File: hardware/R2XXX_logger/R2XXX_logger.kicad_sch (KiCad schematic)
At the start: 34 parts, among them U1 RP2350A, U4 W25Q16JVSS, U7 APS6404L-3SQRx-SN, X1 ABM8-272-T3

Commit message: Throws flatbuf packets
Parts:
- removed CC_19, CC_20: (no value), CC_Misc:CC_Current_Tester, symbol CC_Misc:CC_Current_Tester
- added R4, R5: 10k, Resistor_SMD:R_0603_1608Metric_Pad0.98x0.95mm_HandSolder, symbol Device:R
- added R6, R7: 27, Resistor_SMD:R_0603_1608Metric_Pad0.98x0.95mm_HandSolder, symbol Device:R
- renumbered C55 to C1, C56 to C10, C57 to C11, C58 to C12, C59 to C13, C60 to C14, C29 to C15, C30 to C16, C31 to C17, C34 to C18, C9 to C2, C26 to C3, C28 to C4, C1 to C5, C2 to C6, C42 to C7, C53 to C8, C45 to C9, GND_TP2 to GND_TP1, GND_TP1 to GND_TP2, R14 to R1, R5 to R2, R6 to R3, R3 to R8, U7 to U1, U4 to U2, U1 to U3
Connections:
- net RP_IO is gone; now on net +3.3V: C10.2, C11.2, C12.2, C13.2, C14.2, C9.2, U3.1 (IOVDD), U3.11 (IOVDD), U3.20 (IOVDD), U3.30 (IOVDD), U3.38 (IOVDD), U3.45 (IOVDD)
- net RP_PWR is gone; now on net +3.3V: C7.2, C8.2, R2.1, R3.1, U3.49 (VREG_VIN), U3.53 (USB_OTP_VDD), U3.54 (QSPI_IOVDD)
- net +3.3V: now also R4.2, R5.1
- net USB_DN: now also R7.2
- net USB_DP: now also R6.1; no longer U3.51 (USB_DM)
- net at U3.52 (USB_DP): now also R7.1
- new net: R6.2, U3.51 (USB_DM)
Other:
- moved on the sheet: C10, C11, C12, C13, C14, C9

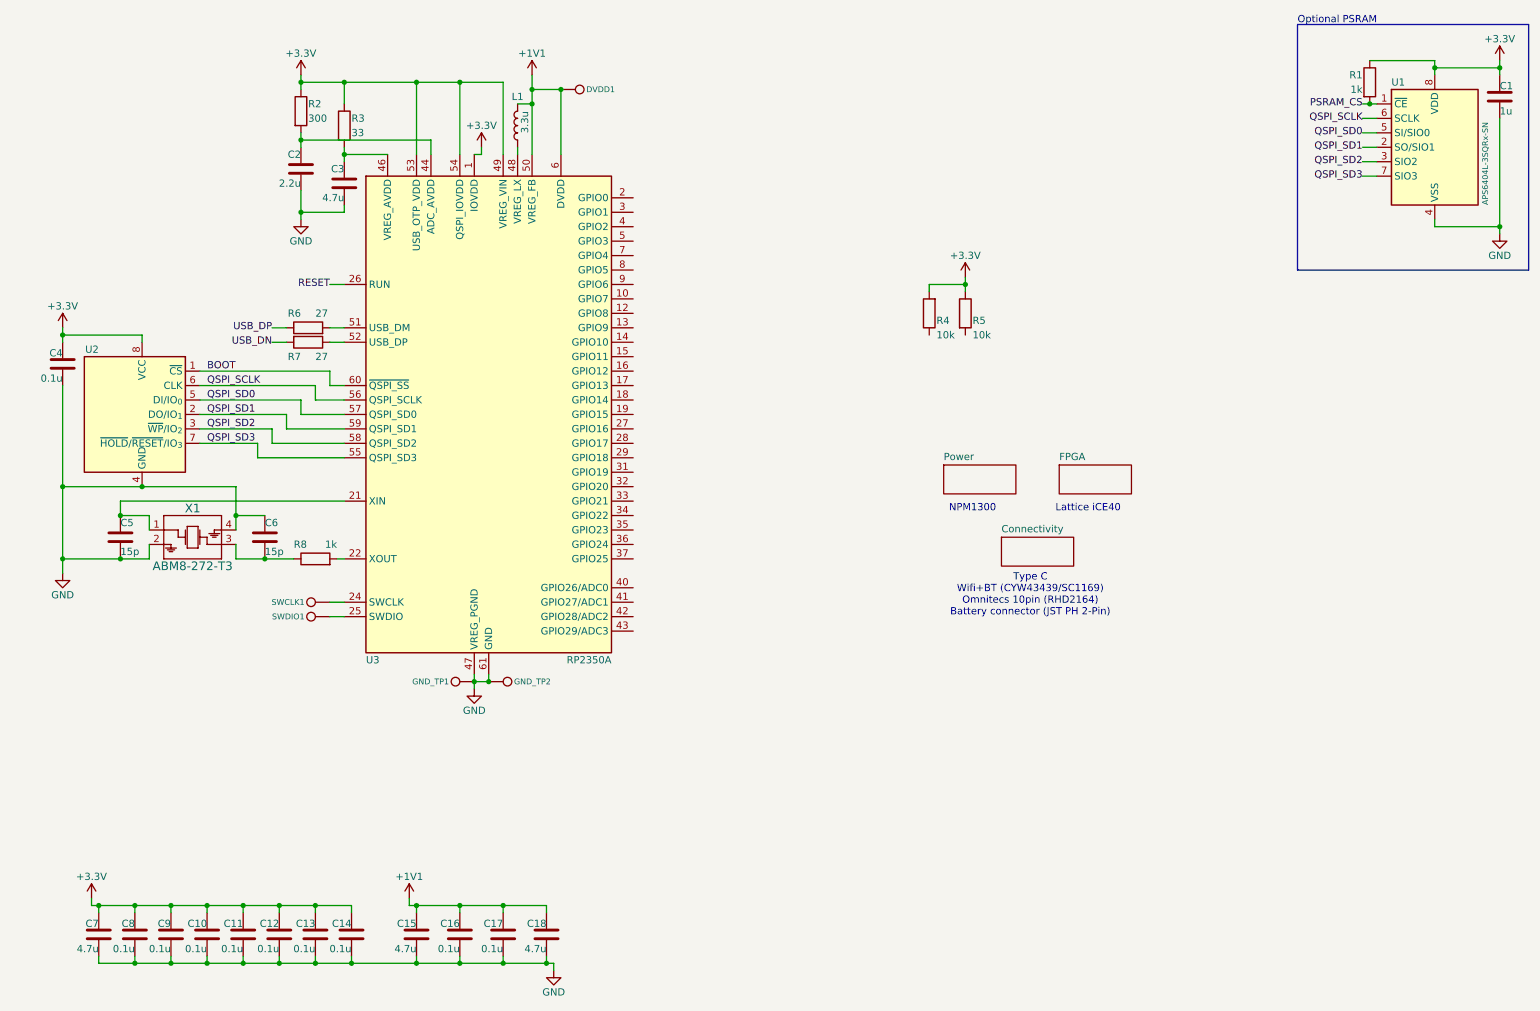
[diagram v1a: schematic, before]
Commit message: Adding the flatbuffer stack causes it to crash
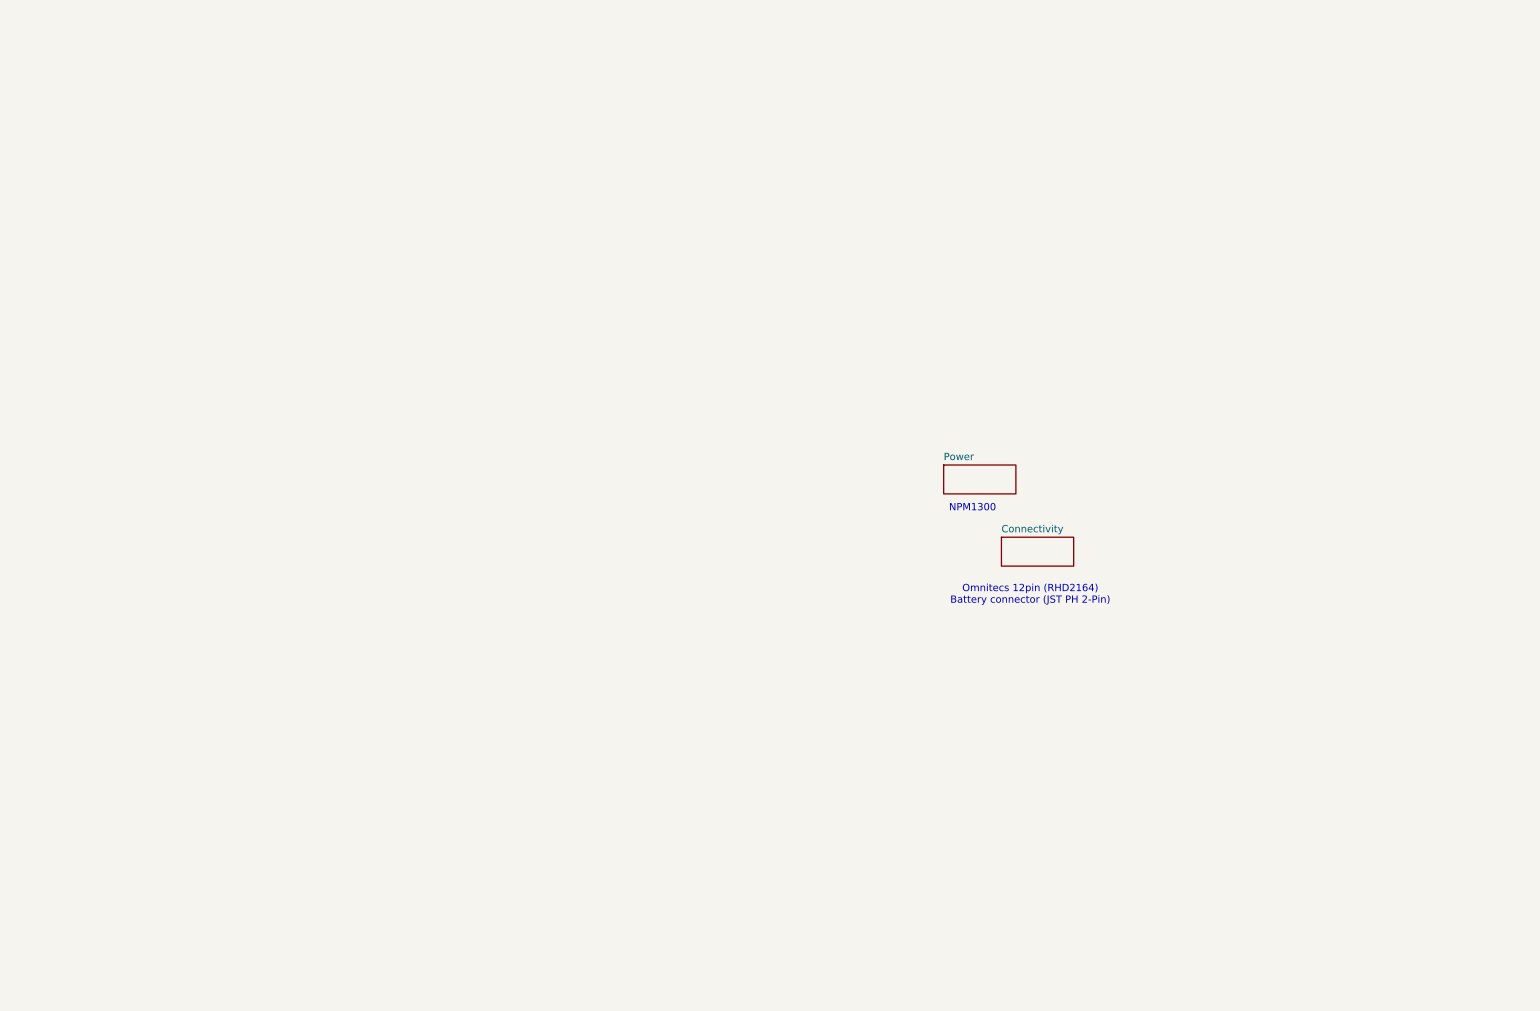
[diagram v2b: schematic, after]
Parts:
- removed C1: 1u, Capacitor_SMD:C_0603_1608Metric_Pad1.08x0.95mm_HandSolder, symbol Device:C
- removed C10, C11, C12, C13, C14, C16, C17, C4, C8, C9: 0.1u, Capacitor_SMD:C_0603_1608Metric_Pad1.08x0.95mm_HandSolder, symbol Device:C
- removed C15, C18, C3, C7: 4.7u, Capacitor_SMD:C_0603_1608Metric_Pad1.08x0.95mm_HandSolder, symbol Device:C
- removed C2: 2.2u, Capacitor_SMD:C_0603_1608Metric_Pad1.08x0.95mm_HandSolder, symbol Device:C
- removed C5, C6: 15p, Capacitor_SMD:C_0603_1608Metric_Pad1.08x0.95mm_HandSolder, symbol Device:C
- removed DVDD1: TestPoint, TestPoint:TestPoint_Pad_D1.0mm, symbol Connector:TestPoint
- removed GND_TP1, GND_TP2, SWCLK1, SWDIO1: TestPoint, TestPoint:TestPoint_THTPad_D2.0mm_Drill1.0mm, symbol Connector:TestPoint
- removed L1: 3.3u, Inductor_SMD:L_0805_2012Metric_Pad1.05x1.20mm_HandSolder, symbol Device:L
- removed R1, R8: 1k, Resistor_SMD:R_0603_1608Metric_Pad0.98x0.95mm_HandSolder, symbol Device:R
- removed R2: 300, Resistor_SMD:R_0603_1608Metric_Pad0.98x0.95mm_HandSolder, symbol Device:R
- removed R3: 33, Resistor_SMD:R_0603_1608Metric_Pad0.98x0.95mm_HandSolder, symbol Device:R
- removed R4, R5: 10k, Resistor_SMD:R_0603_1608Metric_Pad0.98x0.95mm_HandSolder, symbol Device:R
- removed R6, R7: 27, Resistor_SMD:R_0603_1608Metric_Pad0.98x0.95mm_HandSolder, symbol Device:R
- removed U1: APS6404L-3SQRx-SN, Package_SO:SOIC-8_3.9x4.9mm_P1.27mm, symbol Memory_RAM:APS6404L-3SQRx-SN
- removed U2: W25Q16JVSS, Package_SO:SOIC-8_5.3x5.3mm_P1.27mm, symbol Memory_Flash:W25Q16JVSS
- removed U3: RP2350A, Package_DFN_QFN:QFN-60-1EP_7x7mm_P0.4mm_EP3.4x3.4mm, symbol MCU_RaspberryPi:RP2350A
- removed X1: ABM8-272-T3, CC_Misc:ABM8-272-T3_ABR, symbol CC_Misc:ABM8-272-T3
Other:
- removed sheet FPGA
- note added: "Omnitecs 12pin (RHD2164) Battery connector (JST PH 2-Pin)"
- note removed: "Lattice iCE40"
- note removed: "Optional PSRAM"
- note removed: "Type C Wifi+BT (CYW43439/SC1169) Omnitecs 10pin (RHD2164) Battery connector (JST PH 2-Pin)"
